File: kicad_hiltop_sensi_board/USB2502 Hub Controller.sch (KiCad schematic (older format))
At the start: 50 parts, among them U27 USB2502, U7 AT24C02C-SSHM-T, Y1 50ppm 24.000MHZ

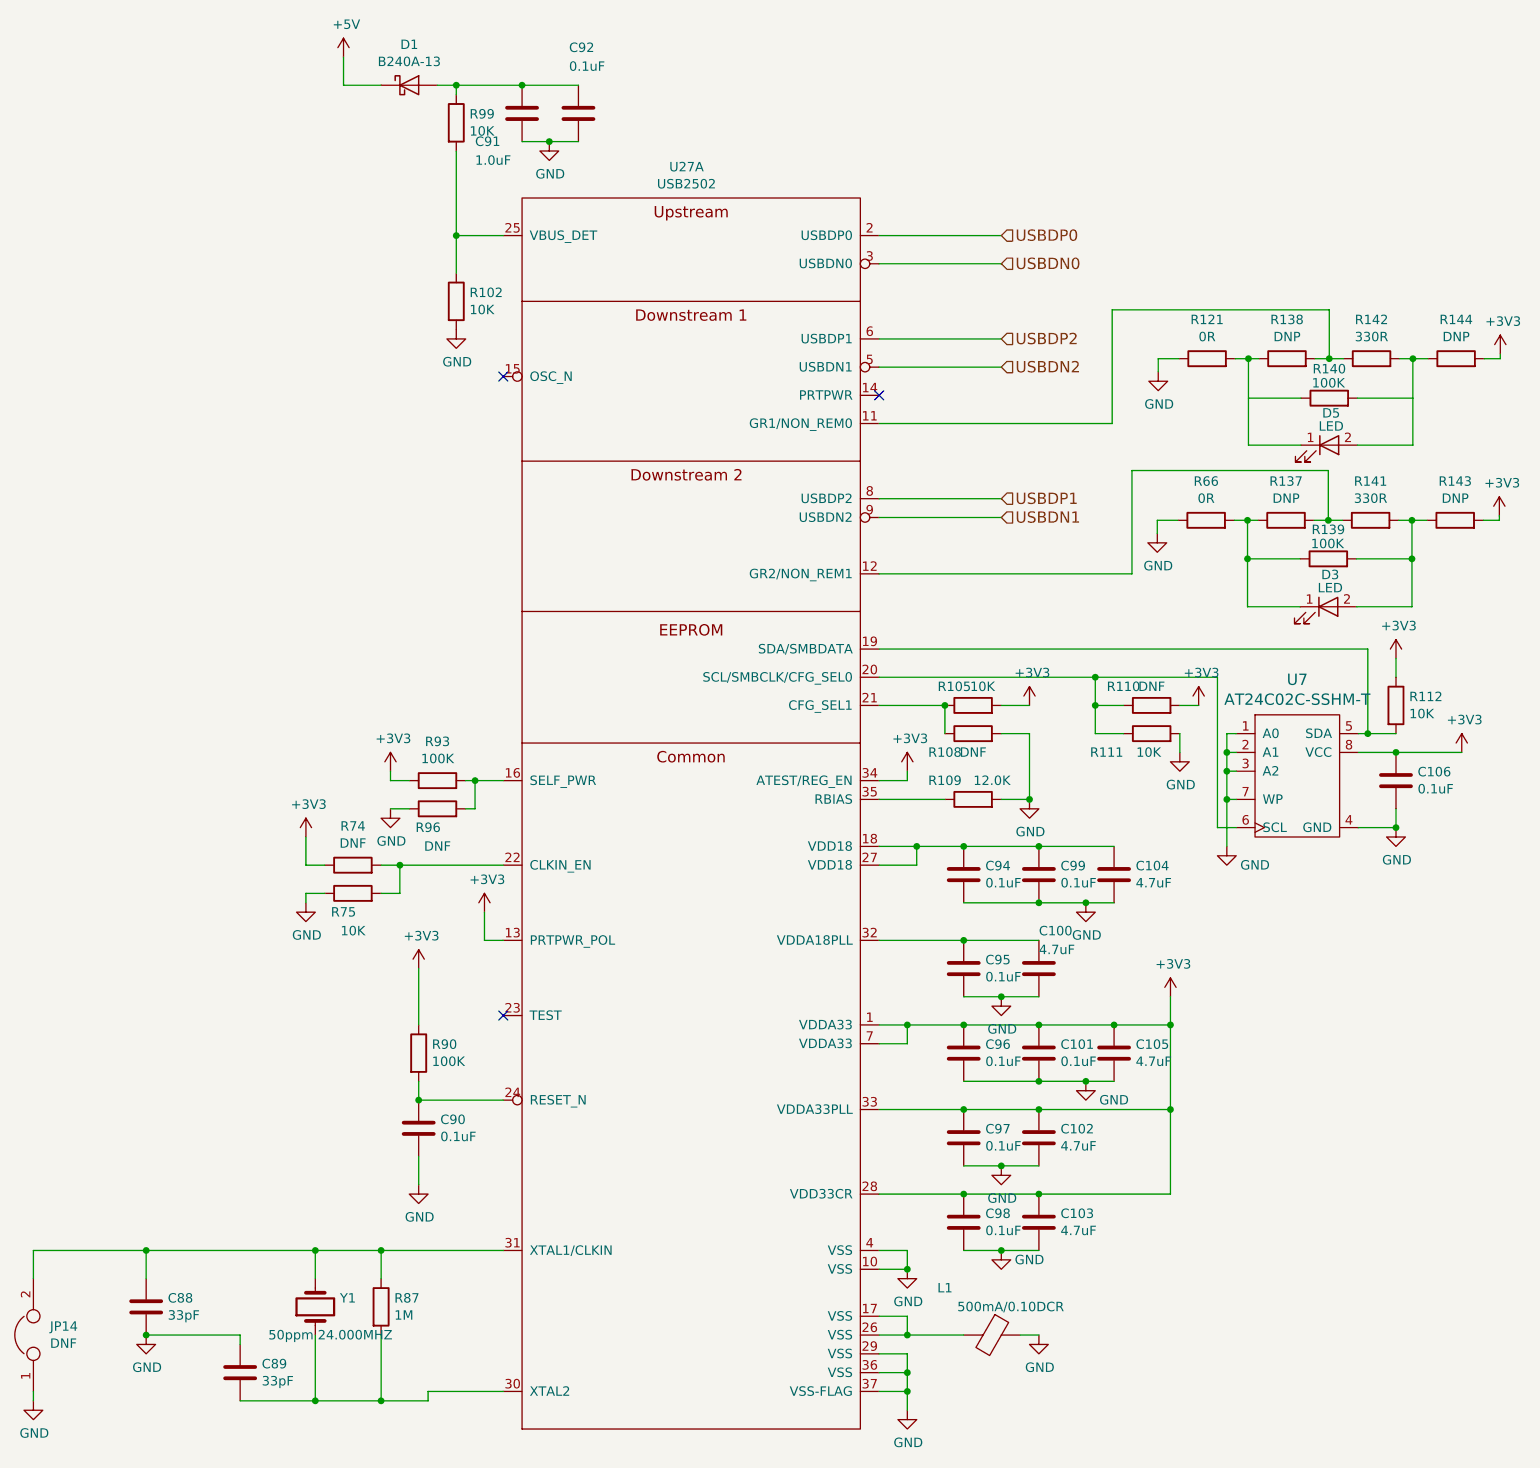
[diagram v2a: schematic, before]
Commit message: Sensi board schematic updated from comments
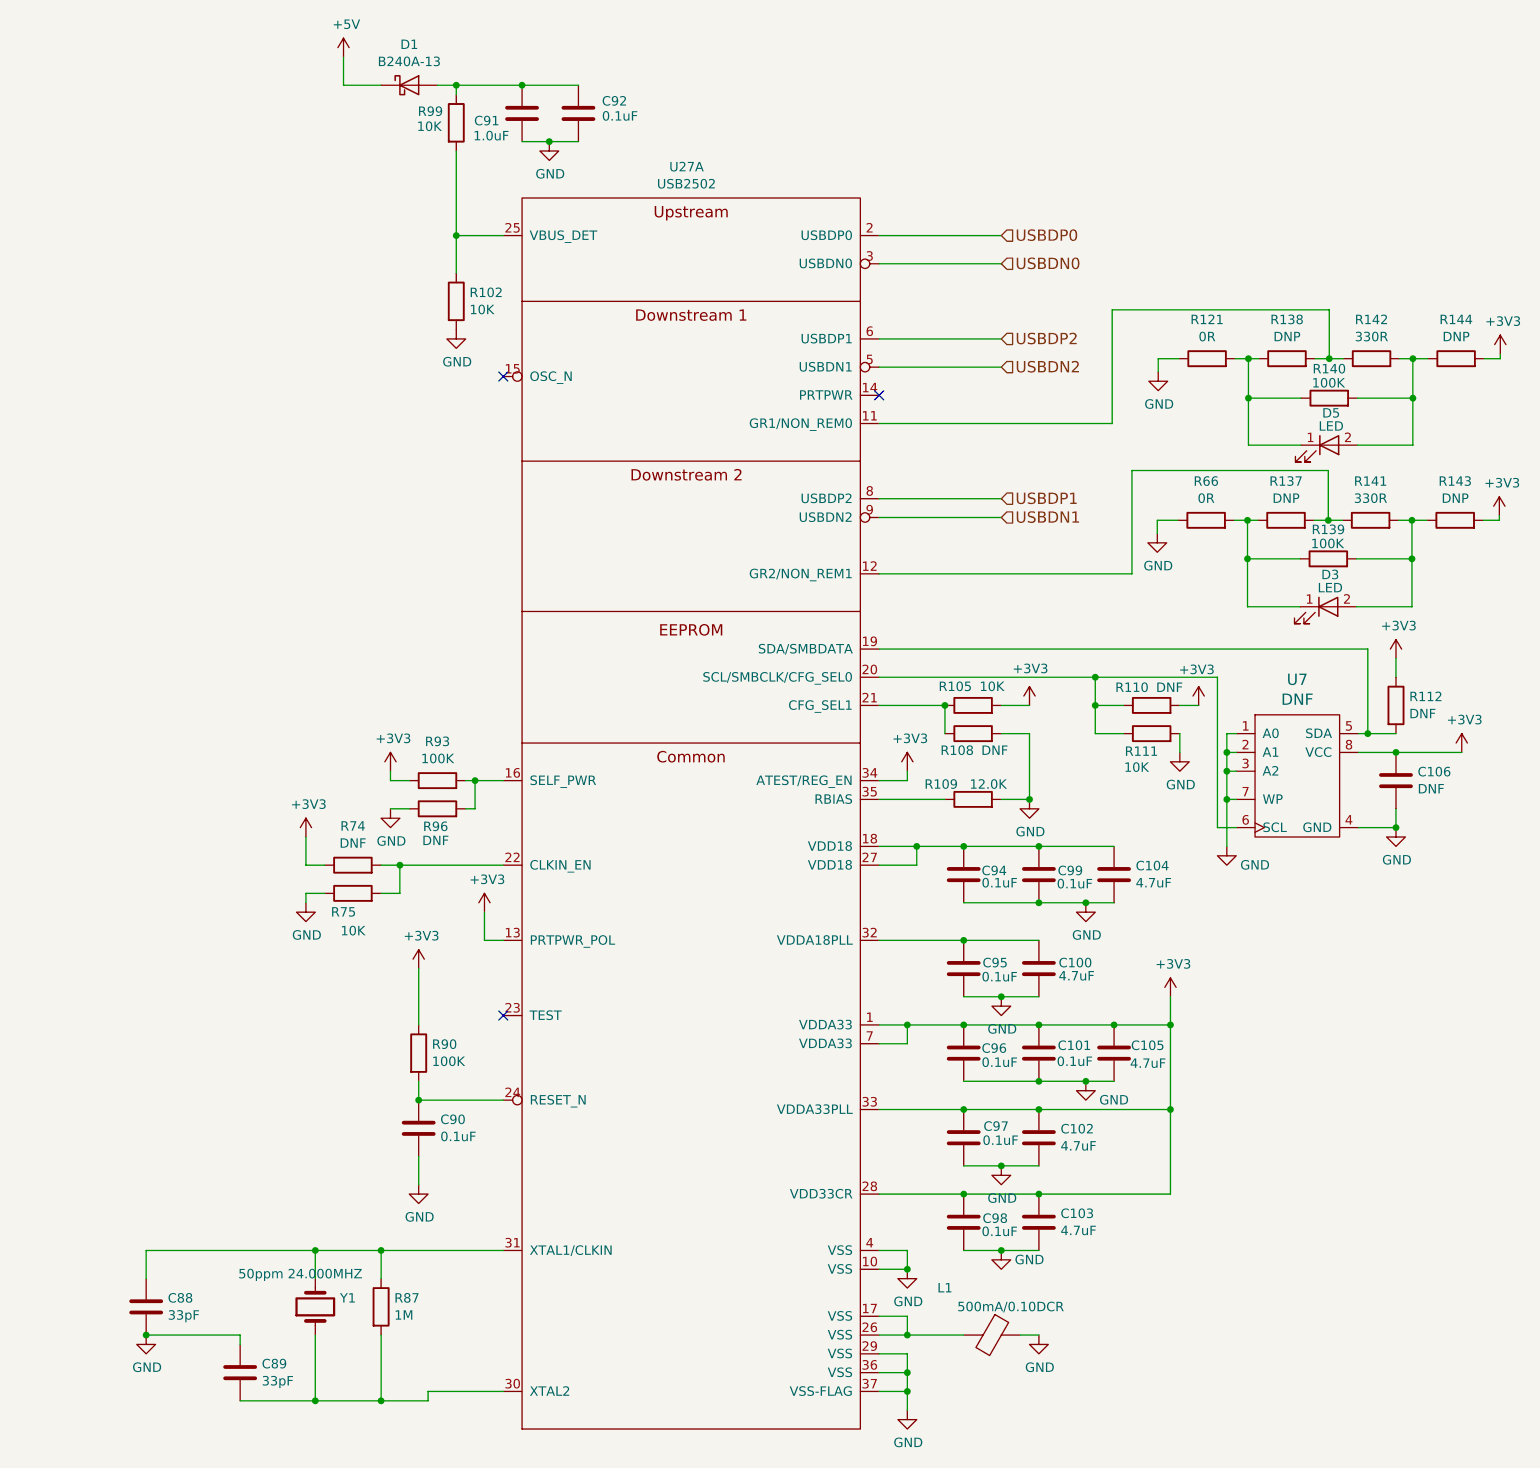
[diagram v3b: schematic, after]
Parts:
- removed JP14: DNF, Connector_PinHeader_2.54mm:PinHeader_1x02_P2.54mm_Vertical, symbol device:Jumper
- C106: value 0.1uF -> DNF
- R112: value 10K -> DNF
- U7: value AT24C02C-SSHM-T -> DNF
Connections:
- net at D5.2 (A), R142.2, R144.1: now also R140.2
- net at D5.1 (K), R121.2, R138.1: now also R140.1
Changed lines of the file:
@@
 $Descr A3 16535 11693
 encoding utf-8
-Sheet 7 11
+Sheet 6 11
 Title ""
 Date "2019-10-01"
@@
 P 4150 8550
 F 0 "Y1" V 4196 8419 50  0000 R CNN
-F 1 "50ppm 24.000MHZ" V 4000 8800 50  0000 R CNN
+F 1 "50ppm 24.000MHZ" V 4325 8960 50  0000 R CNN
 F 2 "Crystal:Crystal_SMD_TXC_7A-2Pin_5x3.2mm" H 4150 8550 50  0001 C CNN
 F 3 "" H 4150 8550 50  0001 C CNN
@@
 U 1 1 5D8F3D03
 P 7650 5500
-F 0 "R108" V 7550 5650 50  0000 C CNN
-F 1 "DNF" V 7550 5500 50  0000 C CNN
+F 0 "R108" V 7560 5585 50  0000 C CNN
+F 1 "DNF" V 7560 5385 50  0000 C CNN
 F 2 "Resistor_SMD:R_0603_1608Metric" V 7580 5500 50  0001 C CNN
 F 3 "" H 7650 5500 50  0001 C CNN
@@
 U 1 1 5D909BDF
 P 8000 7200
-F 0 "C101" H 8115 7246 50  0000 L CNN
-F 1 "0.1uF" H 8115 7155 50  0000 L CNN
+F 0 "C101" H 8100 7240 50  0000 L CNN
+F 1 "0.1uF" H 8095 7155 50  0000 L CNN
 F 2 "Capacitor_SMD:C_0402_1005Metric" H 8038 7050 50  0001 C CNN
 F 3 "" H 8000 7200 50  0001 C CNN
@@
 U 1 1 5D909BE5
 P 8400 7200
-F 0 "C105" H 8515 7246 50  0000 L CNN
-F 1 "4.7uF " H 8515 7155 50  0000 L CNN
+F 0 "C105" H 8490 7240 50  0000 L CNN
+F 1 "4.7uF " H 8485 7145 50  0000 L CNN
 F 2 "Capacitor_SMD:C_0402_1005Metric" H 8438 7050 50  0001 C CNN
 F 3 "" H 8400 7200 50  0001 C CNN
@@
 U 1 1 5D91100B
 P 7600 7200
-F 0 "C96" H 7715 7246 50  0000 L CNN
-F 1 "0.1uF" H 7715 7155 50  0000 L CNN
+F 0 "C96" H 7695 7225 50  0000 L CNN
+F 1 "0.1uF" H 7695 7150 50  0000 L CNN
 F 2 "Capacitor_SMD:C_0402_1005Metric" H 7638 7050 50  0001 C CNN
 F 3 "" H 7600 7200 50  0001 C CNN
@@
 U 1 1 5D919F57
 P 7600 7650
-F 0 "C97" H 7715 7696 50  0000 L CNN
-F 1 "0.1uF" H 7715 7605 50  0000 L CNN
+F 0 "C97" H 7705 7710 50  0000 L CNN
+F 1 "0.1uF" H 7700 7635 50  0000 L CNN
 F 2 "Capacitor_SMD:C_0402_1005Metric" H 7638 7500 50  0001 C CNN
 F 3 "" H 7600 7650 50  0001 C CNN
@@
 U 1 1 5D929924
 P 7600 6750
-F 0 "C95" H 7715 6796 50  0000 L CNN
-F 1 "0.1uF" H 7715 6705 50  0000 L CNN
+F 0 "C95" H 7700 6780 50  0000 L CNN
+F 1 "0.1uF" H 7695 6705 50  0000 L CNN
 F 2 "Capacitor_SMD:C_0402_1005Metric" H 7638 6600 50  0001 C CNN
 F 3 "" H 7600 6750 50  0001 C CNN
@@
 U 1 1 5D92992A
 P 8000 6750
-F 0 "C100" H 8000 6950 50  0000 L CNN
-F 1 "4.7uF " H 8000 6850 50  0000 L CNN
+F 0 "C100" H 8105 6780 50  0000 L CNN
+F 1 "4.7uF " H 8105 6710 50  0000 L CNN
 F 2 "Capacitor_SMD:C_0402_1005Metric" H 8038 6600 50  0001 C CNN
 F 3 "" H 8000 6750 50  0001 C CNN
@@
 U 1 1 5D938ADF
 P 8000 6250
-F 0 "C99" H 8115 6296 50  0000 L CNN
-F 1 "0.1uF" H 8115 6205 50  0000 L CNN
+F 0 "C99" H 8100 6270 50  0000 L CNN
+F 1 "0.1uF" H 8095 6200 50  0000 L CNN
 F 2 "Capacitor_SMD:C_0402_1005Metric" H 8038 6100 50  0001 C CNN
 F 3 "" H 8000 6250 50  0001 C CNN
@@
 U 1 1 5D938AEB
 P 7600 6250
-F 0 "C94" H 7715 6296 50  0000 L CNN
-F 1 "0.1uF" H 7715 6205 50  0000 L CNN
+F 0 "C94" H 7695 6270 50  0000 L CNN
+F 1 "0.1uF" H 7695 6205 50  0000 L CNN
 F 2 "Capacitor_SMD:C_0402_1005Metric" H 7638 6100 50  0001 C CNN
 F 3 "" H 7600 6250 50  0001 C CNN
@@
 P 9900 5750
 F 0 "C106" H 10015 5796 50  0000 L CNN
-F 1 "0.1uF" H 10015 5705 50  0000 L CNN
+F 1 "DNF" H 10015 5705 50  0000 L CNN
 F 2 "Capacitor_SMD:C_0402_1005Metric" H 9938 5600 50  0001 C CNN
 F 3 "" H 9900 5750 50  0001 C CNN
@@
 U 1 1 5D947DA8
 P 7650 5350
-F 0 "R105" V 7750 5450 50  0000 C CNN
-F 1 "10K" V 7750 5300 50  0000 C CNN
+F 0 "R105" V 7750 5445 50  0000 C CNN
+F 1 "10K" V 7750 5250 50  0000 C CNN
 F 2 "Resistor_SMD:R_0603_1608Metric" V 7580 5350 50  0001 C CNN
 F 3 "" H 7650 5350 50  0001 C CNN
@@
 U 1 1 5D949CA8
 P 8600 5500
-F 0 "R111" V 8500 5650 50  0000 L CNN
-F 1 "10K" V 8500 5450 50  0000 L CNN
+F 0 "R111" V 8505 5465 50  0000 L CNN
+F 1 "10K" V 8420 5515 50  0000 L CNN
 F 2 "Resistor_SMD:R_0603_1608Metric" V 8530 5500 50  0001 C CNN
 F 3 "" H 8600 5500 50  0001 C CNN
@@
 U 1 1 5D949CAE
 P 8600 5350
-F 0 "R110" V 8700 5500 50  0000 C CNN
-F 1 "DNF" V 8700 5350 50  0000 C CNN
+F 0 "R110" V 8695 5455 50  0000 C CNN
+F 1 "DNF" V 8695 5255 50  0000 C CNN
 F 2 "Resistor_SMD:R_0603_1608Metric" V 8530 5350 50  0001 C CNN
 F 3 "" H 8600 5350 50  0001 C CNN
@@
 P 9900 5350
 F 0 "R112" H 9970 5396 50  0000 L CNN
-F 1 "10K" H 9970 5305 50  0000 L CNN
+F 1 "DNF" H 9970 5305 50  0000 L CNN
 F 2 "Resistor_SMD:R_0603_1608Metric" V 9830 5350 50  0001 C CNN
 F 3 "" H 9900 5350 50  0001 C CNN
@@
 U 1 1 5D9E4A4E
 P 4800 5900
-F 0 "R96" V 4700 5950 50  0000 C CNN
-F 1 "DNF" V 4600 5900 50  0000 C CNN
+F 0 "R96" V 4705 5910 50  0000 C CNN
+F 1 "DNF" V 4630 5910 50  0000 C CNN
 F 2 "Resistor_SMD:R_0603_1608Metric" V 4730 5900 50  0001 C CNN
 F 3 "" H 4800 5900 50  0001 C CNN
@@
 	1    0    0    -1
 $EndComp
-$Comp
-L device:Jumper JP14
-U 1 1 5DA12303
-P 2650 8700
-F 0 "JP14" V 2696 8612 50  0000 R CNN
-F 1 "DNF" V 2605 8612 50  0000 R CNN
-F 2 "Connector_PinHeader_2.54mm:PinHeader_1x02_P2.54mm_Vertical" H 2650 8700 50  0001 C CNN
-F 3 "" H 2650 8700 50  0001 C CNN
-F 4 "710-002" H 2650 8700 50  0001 C CNN "Devtank"
-	1    2650 8700
-	0    -1   -1   0
-$EndComp
 Wire Wire Line
 	3250 8700 3750 8700
@@
 	4750 9000 5150 9000
 Wire Wire Line
-	2650 8250 2650 8400
-Wire Wire Line
 	3250 8400 3250 8250
-Connection ~ 3250 8250
-Wire Wire Line
-	3250 8250 2650 8250
 Wire Wire Line
 	4150 8400 4150 8250
@@
 U 1 1 5D94B078
 P 7650 5850
-F 0 "R109" V 7750 6000 50  0000 C CNN
-F 1 "12.0K " V 7750 5750 50  0000 C CNN
+F 0 "R109" V 7730 6020 50  0000 C CNN
+F 1 "12.0K " V 7730 5770 50  0000 C CNN
 F 2 "Resistor_SMD:R_0603_1608Metric" V 7580 5850 50  0001 C CNN
 F 3 "" H 7650 5850 50  0001 C CNN
@@
 	1    0    0    -1
 $EndComp
-Wire Wire Line
-	2650 9000 2650 9050
 Wire Wire Line
 	8000 7350 8250 7350
@@
 U 1 1 5D8FF0CE
 P 7600 8100
-F 0 "C98" H 7715 8146 50  0000 L CNN
-F 1 "0.1uF" H 7715 8055 50  0000 L CNN
+F 0 "C98" H 7700 8120 50  0000 L CNN
+F 1 "0.1uF" H 7695 8050 50  0000 L CNN
 F 2 "Capacitor_SMD:C_0402_1005Metric" H 7638 7950 50  0001 C CNN
 F 3 "" H 7600 8100 50  0001 C CNN
@@
 U 1 1 5DCA03F2
 P 5250 2200
-F 0 "C91" H 5000 2050 50  0000 L CNN
-F 1 "1.0uF " H 5000 1950 50  0000 L CNN
+F 0 "C91" H 4995 2160 50  0000 L CNN
+F 1 "1.0uF " H 4990 2080 50  0000 L CNN
 F 2 "Capacitor_SMD:C_0402_1005Metric" H 5288 2050 50  0001 C CNN
 F 3 "" H 5250 2200 50  0001 C CNN
@@
 U 1 1 5DCA2D03
 P 5550 2200
-F 0 "C92" H 5500 2550 50  0000 L CNN
-F 1 "0.1uF" H 5500 2450 50  0000 L CNN
+F 0 "C92" H 5675 2265 50  0000 L CNN
+F 1 "0.1uF" H 5675 2185 50  0000 L CNN
 F 2 "Capacitor_SMD:C_0402_1005Metric" H 5588 2050 50  0001 C CNN
 F 3 "" H 5550 2200 50  0001 C CNN
@@
 U 1 1 5DD02F8D
 P 4900 2250
-F 0 "R99" H 4970 2296 50  0000 L CNN
-F 1 "10K" H 4970 2205 50  0000 L CNN
+F 0 "R99" H 4695 2310 50  0000 L CNN
+F 1 "10K" H 4690 2230 50  0000 L CNN
 F 2 "Resistor_SMD:R_0603_1608Metric" V 4830 2250 50  0001 C CNN
 F 3 "" H 4900 2250 50  0001 C CNN
@@
 	5050 6600 5050 6450
 Connection ~ 3250 8700
-$Comp
-L power:GND #PWR02
-U 1 1 5DC3B84E
-P 2650 9050
-F 0 "#PWR02" H 2650 8800 50  0001 C CNN
-F 1 "GND" H 2655 8877 50  0000 C CNN
-F 2 "" H 2650 9050 50  0001 C CNN
-F 3 "" H 2650 9050 50  0001 C CNN
-	1    2650 9050
-	1    0    0    -1
-$EndComp
 NoConn ~ 7150 3700
 NoConn ~ 5150 3600
@@
 P 9350 5700
 F 0 "U7" H 9375 6187 60  0000 C CNN
-F 1 "AT24C02C-SSHM-T" H 9375 6081 60  0000 C CNN
+F 1 "DNF" H 9375 6081 60  0000 C CNN
 F 2 "Package_SO:SOIC-8_3.9x4.9mm_P1.27mm" H 9300 5150 60  0001 C CNN
 F 3 "" H 9300 5150 60  0001 C CNN
@@
 AR Path="/5D8D08E6/5E674F93" Ref="#PWR0202"  Part="1"
 F 0 "#PWR0202" H 7950 5200 50  0001 C CNN
-F 1 "+3V3" H 7965 5523 50  0000 C CNN
+F 1 "+3V3" H 7955 5545 50  0000 C CNN
 F 2 "" H 7950 5350 50  0001 C CNN
 F 3 "" H 7950 5350 50  0001 C CNN
@@
 AR Path="/5D8D08E6/5E685BFA" Ref="#PWR0205"  Part="1"
 F 0 "#PWR0205" H 8850 5200 50  0001 C CNN
-F 1 "+3V3" H 8865 5523 50  0000 C CNN
+F 1 "+3V3" H 8840 5540 50  0000 C CNN
 F 2 "" H 8850 5350 50  0001 C CNN
 F 3 "" H 8850 5350 50  0001 C CNN
@@
 Wire Wire Line
 	10455 3505 10455 3480
-Wire Wire Line
-	9395 3715 9115 3715
-Wire Wire Line
-	9990 3715 9695 3715
 Connection ~ 9115 3505
 Wire Wire Line
@@
 	9985 4570 9985 4825
 Wire Wire Line
-	9115 3505 9115 3965
-Wire Wire Line
-	9990 3505 9990 3965
+	9115 3505 9115 3715
+Wire Wire Line
+	9990 3505 9990 3715
+Wire Wire Line
+	9695 3715 9990 3715
+Connection ~ 9990 3715
+Wire Wire Line
+	9990 3715 9990 3965
+Wire Wire Line
+	9395 3715 9115 3715
+Connection ~ 9115 3715
+Wire Wire Line
+	9115 3715 9115 3965
 $EndSCHEMATC

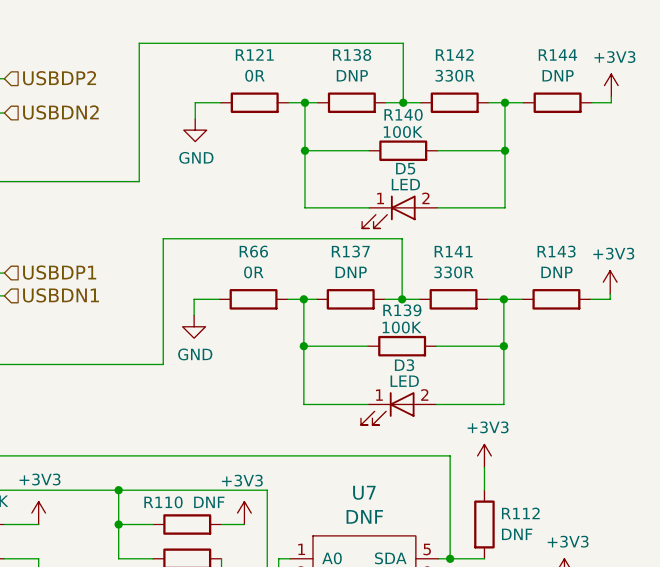
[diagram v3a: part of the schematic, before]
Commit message: Updated sensi board layout
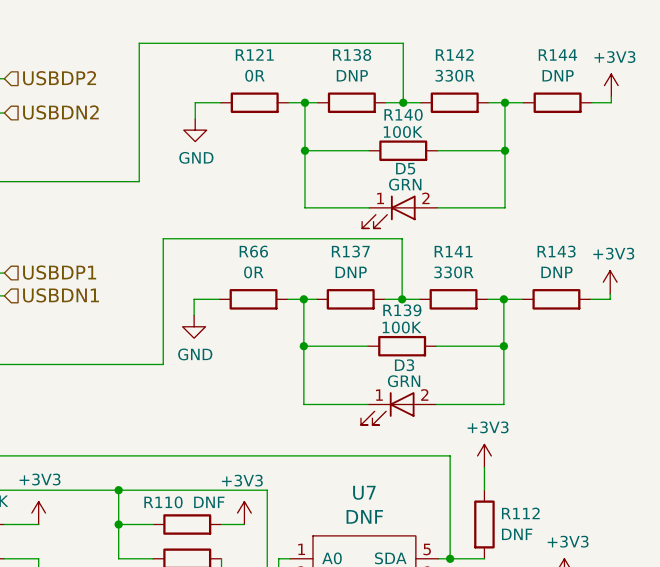
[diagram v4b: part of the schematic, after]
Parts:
- D3, D5: value LED -> GRN; footprint (none) -> LED_SMD:LED_0603_1608Metric
- R121, R137, R138, R139, R140, R141, R142, R143, R144, R66: footprint (none) -> Resistor_SMD:R_0603_1608Metric
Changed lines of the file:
@@
 $Descr A3 16535 11693
 encoding utf-8
-Sheet 6 11
+Sheet 5 11
 Title ""
 Date "2019-10-01"
@@
 F 0 "R143" V 10422 4365 50  0000 C CNN
 F 1 "DNP" V 10331 4365 50  0000 C CNN
-F 2 "" V 10145 4365 50  0001 C CNN
+F 2 "Resistor_SMD:R_0603_1608Metric" V 10145 4365 50  0001 C CNN
 F 3 "" H 10215 4365 50  0001 C CNN
 	1    10215 4365
@@
 F 0 "R141" V 9972 4365 50  0000 C CNN
 F 1 "330R" V 9881 4365 50  0000 C CNN
-F 2 "" V 9695 4365 50  0001 C CNN
+F 2 "Resistor_SMD:R_0603_1608Metric" V 9695 4365 50  0001 C CNN
 F 3 "" H 9765 4365 50  0001 C CNN
 	1    9765 4365
@@
 F 0 "R137" V 9522 4365 50  0000 C CNN
 F 1 "DNP" V 9431 4365 50  0000 C CNN
-F 2 "" V 9245 4365 50  0001 C CNN
+F 2 "Resistor_SMD:R_0603_1608Metric" V 9245 4365 50  0001 C CNN
 F 3 "" H 9315 4365 50  0001 C CNN
 	1    9315 4365
@@
 F 0 "R66" V 9097 4365 50  0000 C CNN
 F 1 "0R" V 9006 4365 50  0000 C CNN
-F 2 "" V 8820 4365 50  0001 C CNN
+F 2 "Resistor_SMD:R_0603_1608Metric" V 8820 4365 50  0001 C CNN
 F 3 "" H 8890 4365 50  0001 C CNN
 	1    8890 4365
@@
 F 0 "R139" V 9695 4570 50  0000 C CNN
 F 1 "100K" V 9620 4575 50  0000 C CNN
-F 2 "" V 9470 4570 50  0001 C CNN
+F 2 "Resistor_SMD:R_0603_1608Metric" V 9470 4570 50  0001 C CNN
 F 3 "" H 9540 4570 50  0001 C CNN
 	1    9540 4570
@@
 P 9540 4825
 F 0 "D3" H 9550 4995 50  0000 C CNN
-F 1 "LED" H 9550 4925 50  0000 C CNN
-F 2 "" H 9540 4825 50  0001 C CNN
+F 1 "GRN" H 9550 4925 50  0000 C CNN
+F 2 "LED_SMD:LED_0603_1608Metric" H 9540 4825 50  0001 C CNN
 F 3 "~" H 9540 4825 50  0001 C CNN
 	1    9540 4825
@@
 F 0 "R144" V 10427 3505 50  0000 C CNN
 F 1 "DNP" V 10336 3505 50  0000 C CNN
-F 2 "" V 10150 3505 50  0001 C CNN
+F 2 "Resistor_SMD:R_0603_1608Metric" V 10150 3505 50  0001 C CNN
 F 3 "" H 10220 3505 50  0001 C CNN
 	1    10220 3505
@@
 F 0 "R142" V 9977 3505 50  0000 C CNN
 F 1 "330R" V 9886 3505 50  0000 C CNN
-F 2 "" V 9700 3505 50  0001 C CNN
+F 2 "Resistor_SMD:R_0603_1608Metric" V 9700 3505 50  0001 C CNN
 F 3 "" H 9770 3505 50  0001 C CNN
 	1    9770 3505
@@
 F 0 "R138" V 9527 3505 50  0000 C CNN
 F 1 "DNP" V 9436 3505 50  0000 C CNN
-F 2 "" V 9250 3505 50  0001 C CNN
+F 2 "Resistor_SMD:R_0603_1608Metric" V 9250 3505 50  0001 C CNN
 F 3 "" H 9320 3505 50  0001 C CNN
 	1    9320 3505
@@
 F 0 "R121" V 9102 3505 50  0000 C CNN
 F 1 "0R" V 9011 3505 50  0000 C CNN
-F 2 "" V 8825 3505 50  0001 C CNN
+F 2 "Resistor_SMD:R_0603_1608Metric" V 8825 3505 50  0001 C CNN
 F 3 "" H 8895 3505 50  0001 C CNN
 	1    8895 3505
@@
 F 0 "R140" V 9700 3715 50  0000 C CNN
 F 1 "100K" V 9625 3720 50  0000 C CNN
-F 2 "" V 9475 3715 50  0001 C CNN
+F 2 "Resistor_SMD:R_0603_1608Metric" V 9475 3715 50  0001 C CNN
 F 3 "" H 9545 3715 50  0001 C CNN
 	1    9545 3715
@@
 P 9545 3965
 F 0 "D5" H 9555 4135 50  0000 C CNN
-F 1 "LED" H 9555 4065 50  0000 C CNN
-F 2 "" H 9545 3965 50  0001 C CNN
+F 1 "GRN" H 9555 4065 50  0000 C CNN
+F 2 "LED_SMD:LED_0603_1608Metric" H 9545 3965 50  0001 C CNN
 F 3 "~" H 9545 3965 50  0001 C CNN
 	1    9545 3965
